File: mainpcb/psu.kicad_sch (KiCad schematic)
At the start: 15 parts, among them J5 8PCV-06-006, U3 LM2678T-12, U4 LM2678T-5

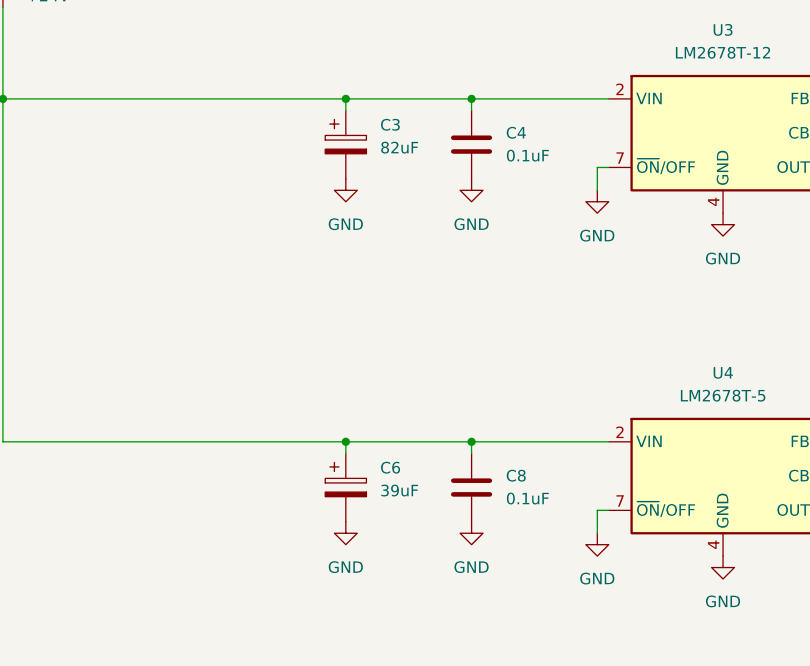
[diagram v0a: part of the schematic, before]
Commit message: Version 1 AS-BUILT commit
This commit has the schematics of version 1 of the system AS IT WAS BUILT
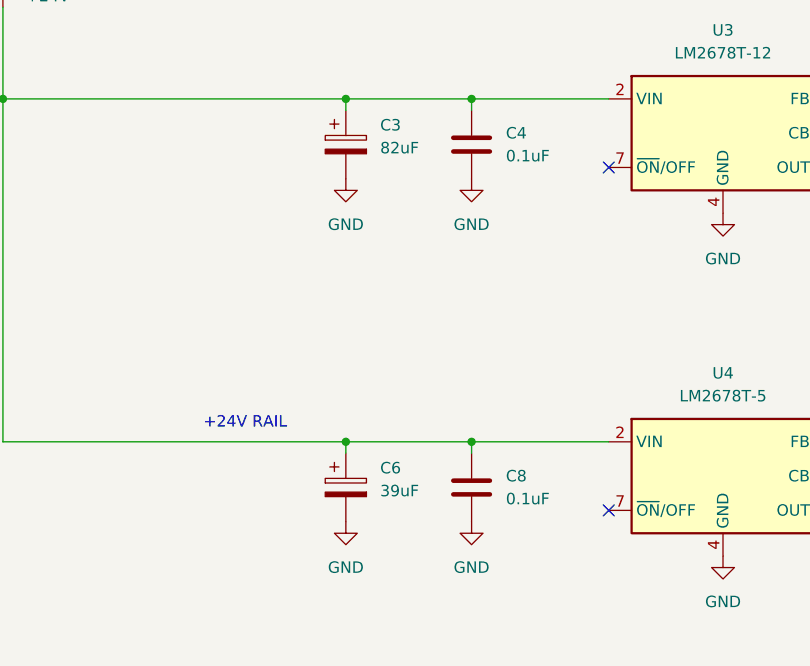
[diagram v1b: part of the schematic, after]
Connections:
- net GND: no longer U3.7 (~{ON}/OFF), U4.7 (~{ON}/OFF)
- no-connect marks 0 -> 2
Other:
- note added: "+24V RAIL"
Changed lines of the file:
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@@
 		(color 0 0 0 0)
 	)
+	(no_connect
+		(at 156.21 119.38)
+	)
+	(no_connect
+		(at 156.21 81.28)
+	)
 	(wire
 		(pts
@@
 	(wire
 		(pts
-			(xy 154.94 121.92) (xy 154.94 119.38)
-		)
-		(stroke
-			(width 0)
-			(type default)
-		)
-	)
-	(wire
-		(pts
 			(xy 88.9 73.66) (xy 127 73.66)
 		)
@@
 	(wire
 		(pts
-			(xy 154.94 83.82) (xy 154.94 81.28)
-		)
-		(stroke
-			(width 0)
-			(type default)
-		)
-	)
-	(wire
-		(pts
 			(xy 127 111.76) (xy 127 113.03)
 		)
@@
 	(wire
 		(pts
-			(xy 154.94 81.28) (xy 156.21 81.28)
-		)
-		(stroke
-			(width 0)
-			(type default)
-		)
-	)
-	(wire
-		(pts
 			(xy 218.44 119.38) (xy 243.84 119.38)
 		)
@@
 	(wire
 		(pts
-			(xy 154.94 119.38) (xy 156.21 119.38)
-		)
-		(stroke
-			(width 0)
-			(type default)
-		)
-	)
-	(wire
-		(pts
 			(xy 60.96 76.2) (xy 64.77 76.2)
 		)
@@
 		(exclude_from_sim no)
 		(at 57.404 51.054 0)
+		(effects
+			(font
+				(size 1.27 1.27)
+			)
+		)
+	)
+	(text "+24V RAIL\n"
+		(exclude_from_sim no)
+		(at 115.824 109.728 0)
 		(effects
 			(font
@@
 	)
 	(symbol
-		(lib_id "power:GND")
-		(at 154.94 83.82 0)
-		(mirror y)
-		(unit 1)
-		(exclude_from_sim no)
-		(in_bom yes)
-		(on_board yes)
-		(dnp no)
-		(property "Reference" "#PWR029"
-			(at 154.94 90.17 0)
-			(effects
-				(font
-					(size 1.27 1.27)
-				)
-				(hide yes)
-			)
-		)
-		(property "Value" "GND"
-			(at 154.94 88.9 0)
-			(effects
-				(font
-					(size 1.27 1.27)
-				)
-			)
-		)
-		(property "Footprint" ""
-			(at 154.94 83.82 0)
-			(effects
-				(font
-					(size 1.27 1.27)
-				)
-				(hide yes)
-			)
-		)
-		(property "Datasheet" ""
-			(at 154.94 83.82 0)
-			(effects
-				(font
-					(size 1.27 1.27)
-				)
-				(hide yes)
-			)
-		)
-		(property "Description" "Power symbol creates a global label with name \"GND\" , ground"
-			(at 154.94 83.82 0)
-			(effects
-				(font
-					(size 1.27 1.27)
-				)
-				(hide yes)
-			)
-		)
-		(pin "1"
-		)
-		(instances
-			(project "mainpcb"
-				(path "/8e899647-a0f4-47d2-9d4a-2e9de2221eca/9d696eb8-716e-4588-b1b5-ec895711ca90"
-					(reference "#PWR029")
-					(unit 1)
-				)
-			)
-		)
-	)
-	(symbol
 		(lib_id "Device:C_Polarized")
 		(at 218.44 124.46 0)
@@
 					(unit 1)
 				)
-			)
-		)
-	)
-	(symbol
-		(lib_id "power:GND")
-		(at 154.94 121.92 0)
-		(mirror y)
-		(unit 1)
-		(exclude_from_sim no)
-		(in_bom yes)
-		(on_board yes)
-		(dnp no)
-		(property "Reference" "#PWR034"
-			(at 154.94 128.27 0)
-			(effects
-				(font
-					(size 1.27 1.27)
-				)
-				(hide yes)
-			)
-		)
-		(property "Value" "GND"
-			(at 154.94 127 0)
-			(effects
-				(font
-					(size 1.27 1.27)
-				)
-			)
-		)
-		(property "Footprint" ""
-			(at 154.94 121.92 0)
-			(effects
-				(font
-					(size 1.27 1.27)
-				)
-				(hide yes)
-			)
-		)
-		(property "Datasheet" ""
-			(at 154.94 121.92 0)
-			(effects
-				(font
-					(size 1.27 1.27)
-				)
-				(hide yes)
-			)
-		)
-		(property "Description" "Power symbol creates a global label with name \"GND\" , ground"
-			(at 154.94 121.92 0)
-			(effects
-				(font
-					(size 1.27 1.27)
-				)
-				(hide yes)
-			)
-		)
-		(pin "1"
-		)
-		(instances
-			(project "mainpcb"
-				(path "/8e899647-a0f4-47d2-9d4a-2e9de2221eca/9d696eb8-716e-4588-b1b5-ec895711ca90"
-					(reference "#PWR034")
-					(unit 1)
-				)

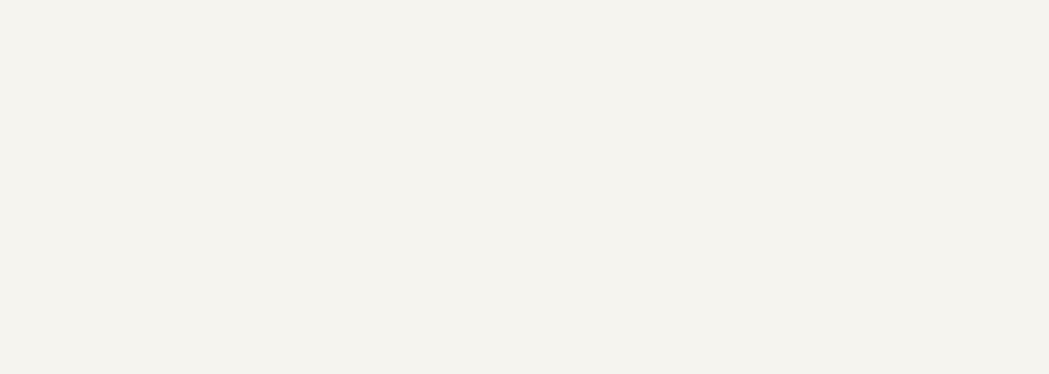
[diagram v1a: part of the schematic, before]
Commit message: Added drawing information boxes
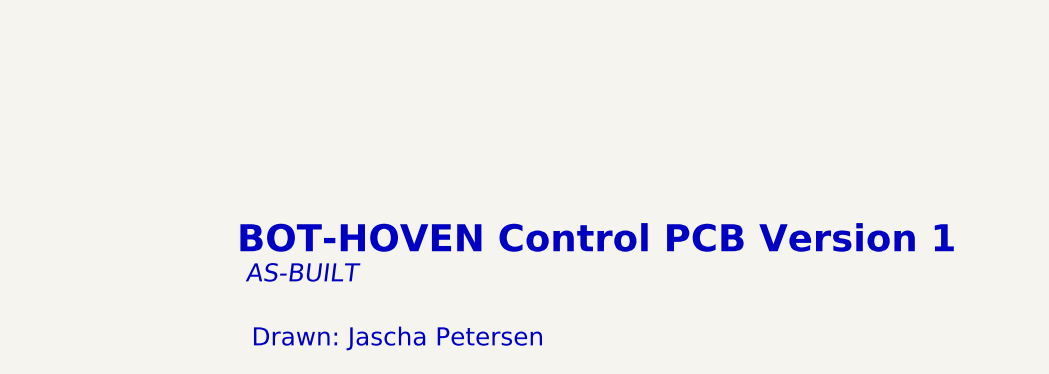
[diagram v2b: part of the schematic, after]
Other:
- note added: "AS-BUILT"
- note added: "BOT-HOVEN Control PCB Version 1"
- note added: "Drawn: Jascha Petersen"
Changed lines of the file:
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@@
+		)
+	)
+	(text "Drawn: Jascha Petersen"
+		(exclude_from_sim no)
+		(at 195.58 179.832 0)
+		(effects
+			(font
+				(size 2 2)
+			)
+		)
+	)
+	(text "AS-BUILT"
+		(exclude_from_sim no)
+		(at 184.912 172.72 0)
+		(effects
+			(font
+				(size 2 2)
+				(italic yes)
+			)
 		)
 	)
@@
 			)
 		)
+	)
+	(text "BOT-HOVEN Control PCB Version 1"
+		(exclude_from_sim no)
+		(at 217.678 168.91 0)
+		(effects
+			(font
+				(size 3 3)
+				(thickness 0.6)
+				(bold yes)
+			)
+		)

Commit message: Added PDF schematic exports
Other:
- title: (none) -> Control PCB PSU
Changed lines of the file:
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@@
 	(generator_version "8.0")
 	(paper "A4")
+	(title_block
+		(title "Control PCB PSU")
+	)
 	(junction
 		(at 218.44 119.38)
